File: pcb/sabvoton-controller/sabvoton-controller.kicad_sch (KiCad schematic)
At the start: 43 parts, among them J1 CONTROLLER_HALL, J2 CONN_MAIN, J3 ENGINE_HALL, J4 DISPLAY_CONNECTOR, Q1 BSS123, Q2 BSS123, Q3 BSS123, U1 ESP32-WROOM-32, U2 XL7015E1, U3 XL7015E1, U4 NCP1117-3.3_SOT223, U5 LM1117-1.8, U6 BTS4140N, U7 LM358

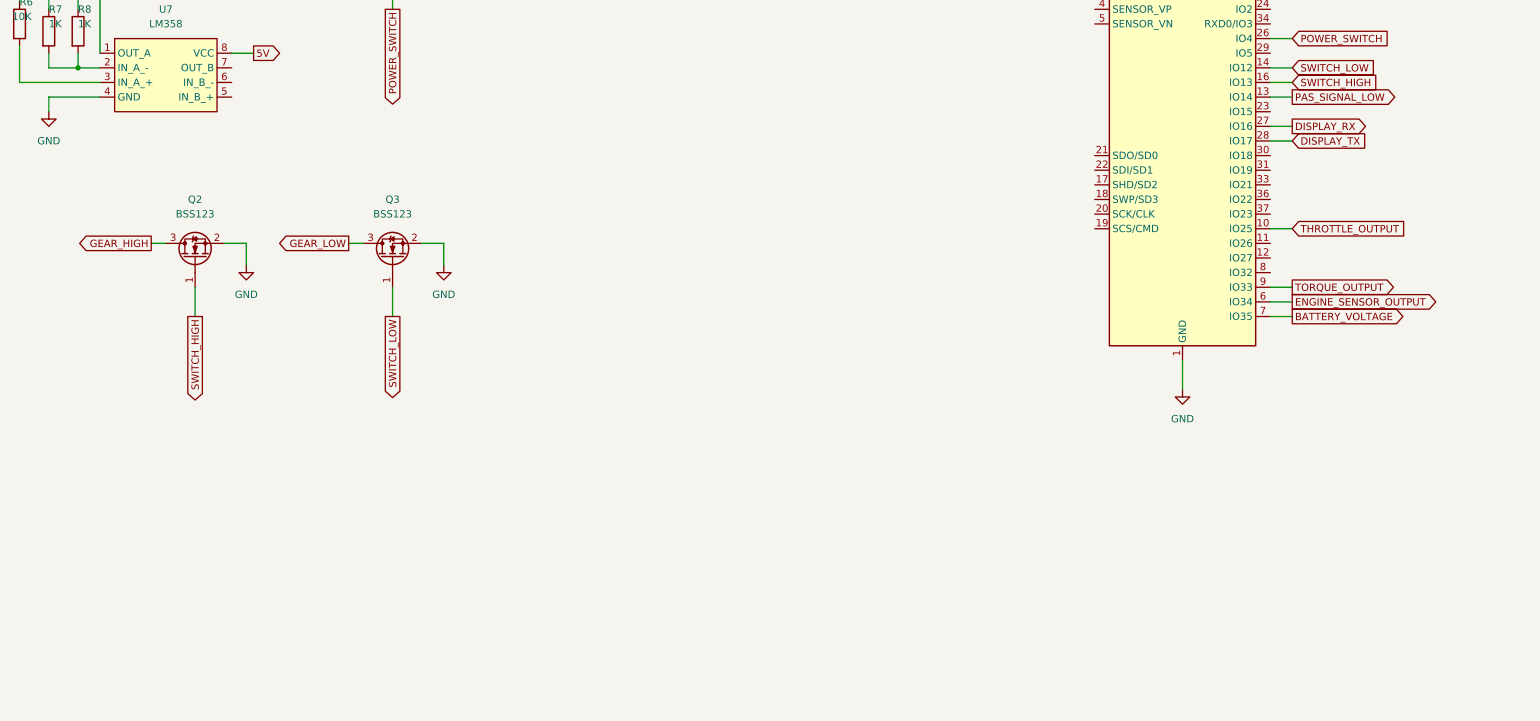
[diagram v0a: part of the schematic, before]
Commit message: Added soft start switch
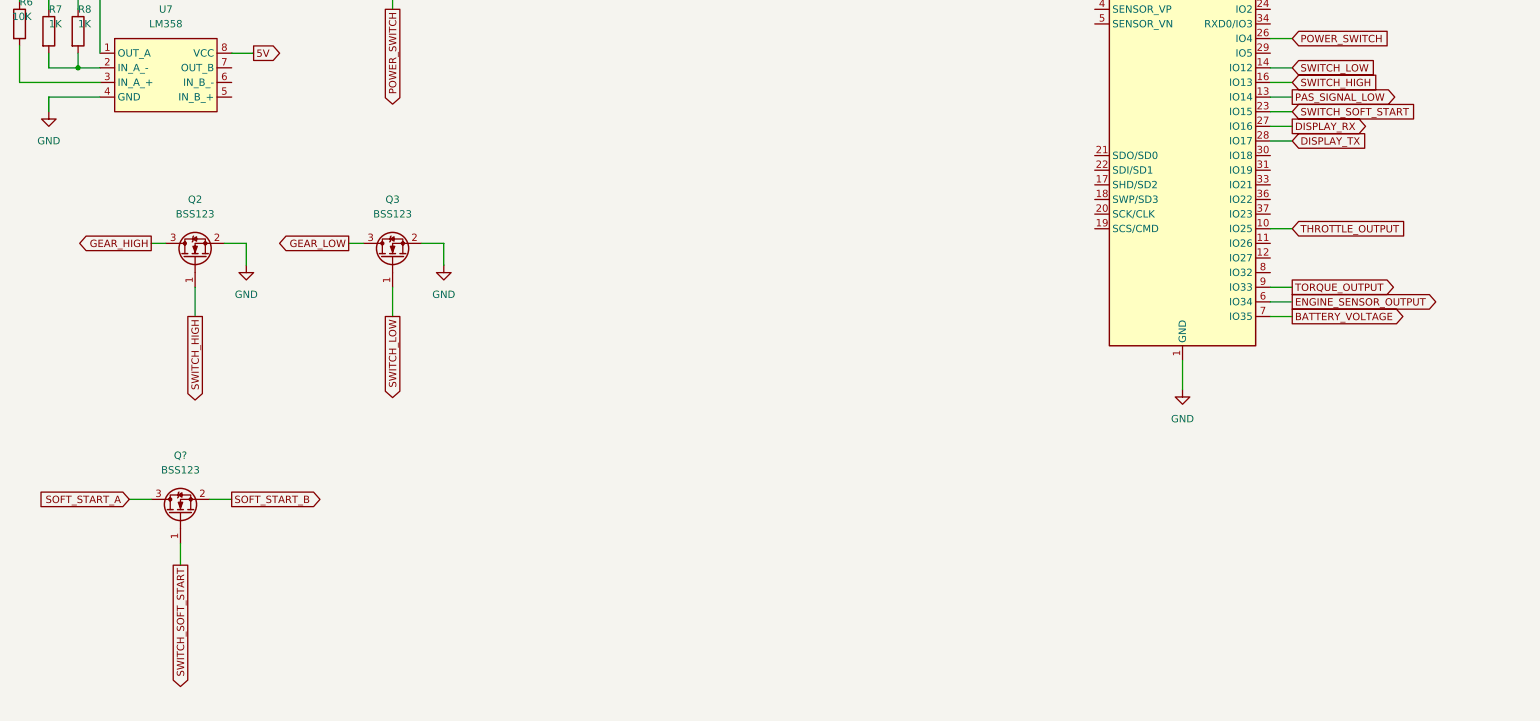
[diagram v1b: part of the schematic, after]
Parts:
- added Q?: BSS123, Package_TO_SOT_SMD:SOT-23, symbol Transistor_FET:BSS123
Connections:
- net SOFT_START_A: now also Q?.3 (D)
- net SOFT_START_B: now also Q?.2 (S)
- net SWITCH_SOFT_START: now reaches U1.23 (IO15)
- net SWITCH_SOFT_START: now also Q?.1 (G)
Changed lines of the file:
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@@
+    (stroke (width 0) (type default) (color 0 0 0 0))
+  )
+  (wire (pts (xy 209.55 219.71) (xy 213.36 219.71))
     (stroke (width 0) (type default) (color 0 0 0 0))
   )
@@
     (stroke (width 0) (type default) (color 0 0 0 0))
   )
+  (wire (pts (xy 204.47 227.33) (xy 204.47 231.14))
+    (stroke (width 0) (type default) (color 0 0 0 0))
+  )
   (wire (pts (xy 339.09 66.04) (xy 339.09 71.12))
     (stroke (width 0) (type default) (color 0 0 0 0))
@@
     (stroke (width 0) (type default) (color 0 0 0 0))
   )
+  (wire (pts (xy 393.7 152.4) (xy 397.51 152.4))
+    (stroke (width 0) (type default) (color 0 0 0 0))
+  )
   (wire (pts (xy 336.55 63.5) (xy 336.55 48.26))
     (stroke (width 0) (type default) (color 0 0 0 0))
@@
     (stroke (width 0) (type default) (color 0 0 0 0))
   )
+  (wire (pts (xy 195.58 219.71) (xy 199.39 219.71))
+    (stroke (width 0) (type default) (color 0 0 0 0))
+  )
   (wire (pts (xy 378.46 118.11) (xy 378.46 124.46))
     (stroke (width 0) (type default) (color 0 0 0 0))
@@
     )
   )
+  (global_label "SWITCH_SOFT_START" (shape input) (at 397.51 152.4 0) (fields_autoplaced)
+    (effects (font (size 1.27 1.27)) (justify left))
+    (property "Intersheet References" "${INTERSHEET_REFS}" (id 0) (at 418.7917 152.3206 0)
+      (effects (font (size 1.27 1.27)) (justify left) hide)
+    )
+  )
   (global_label "DISPLAY_TX" (shape output) (at 285.75 50.8 270) (fields_autoplaced)
     (effects (font (size 1.27 1.27)) (justify right))
@@
     )
   )
+  (global_label "SWITCH_SOFT_START" (shape output) (at 204.47 231.14 270) (fields_autoplaced)
+    (effects (font (size 1.27 1.27)) (justify right))
+    (property "Intersheet References" "${INTERSHEET_REFS}" (id 0) (at 204.3906 252.4217 90)
+      (effects (font (size 1.27 1.27)) (justify right) hide)
+    )
+  )
   (global_label "3.3V" (shape output) (at 378.46 118.11 90) (fields_autoplaced)
     (effects (font (size 1.27 1.27)) (justify left))
@@
     )
   )
+  (global_label "SOFT_START_A" (shape input) (at 195.58 219.71 180) (fields_autoplaced)
+    (effects (font (size 1.27 1.27)) (justify right))
+    (property "Intersheet References" "${INTERSHEET_REFS}" (id 0) (at 180.0436 219.6306 0)
+      (effects (font (size 1.27 1.27)) (justify right) hide)
+    )
+  )
   (global_label "PAS_SIGNAL" (shape output) (at 508 147.32 180) (fields_autoplaced)
     (effects (font (size 1.27 1.27)) (justify right))
@@
     (effects (font (size 1.27 1.27)) (justify left))
     (property "Intersheet References" "${INTERSHEET_REFS}" (id 0) (at 545.3079 147.2406 0)
+      (effects (font (size 1.27 1.27)) (justify left) hide)
+    )
+  )
+  (global_label "SOFT_START_B" (shape output) (at 213.36 219.71 0) (fields_autoplaced)
+    (effects (font (size 1.27 1.27)) (justify left))
+    (property "Intersheet References" "${INTERSHEET_REFS}" (id 0) (at 229.0779 219.6306 0)
       (effects (font (size 1.27 1.27)) (justify left) hide)
     )
@@
     (pin "3")
     (pin "4")
+  )
+  (symbol (lib_id "Transistor_FET:BSS123") (at 204.47 222.25 90) (unit 1)
+    (in_bom yes) (on_board yes) (fields_autoplaced)
+    (property "Reference" "Q?" (id 0) (at 204.47 212.09 90))
+    (property "Value" "BSS123" (id 1) (at 204.47 214.63 90))
+    (property "Footprint" "Package_TO_SOT_SMD:SOT-23" (id 2) (at 206.375 217.17 0)
+      (effects (font (size 1.27 1.27) italic) (justify left) hide)
+    )
+    (property "Datasheet" "http://www.diodes.com/assets/Datasheets/ds30366.pdf" (id 3) (at 204.47 222.25 0)
+      (effects (font (size 1.27 1.27)) (justify left) hide)
+    )
+    (pin "1")
+    (pin "2")
+    (pin "3")
   )
   (symbol (lib_id "Device:C") (at 544.83 104.14 0) (unit 1)
@@
       (reference "Q3") (unit 1) (value "BSS123") (footprint "Package_TO_SOT_SMD:SOT-23")
     )
+    (path "/733e1eb3-afcc-4a44-afac-d7ce4b6dac88"
+      (reference "Q?") (unit 1) (value "BSS123") (footprint "Package_TO_SOT_SMD:SOT-23")
+    )
     (path "/3c54a24c-10be-4236-a15f-1623c52b157c"

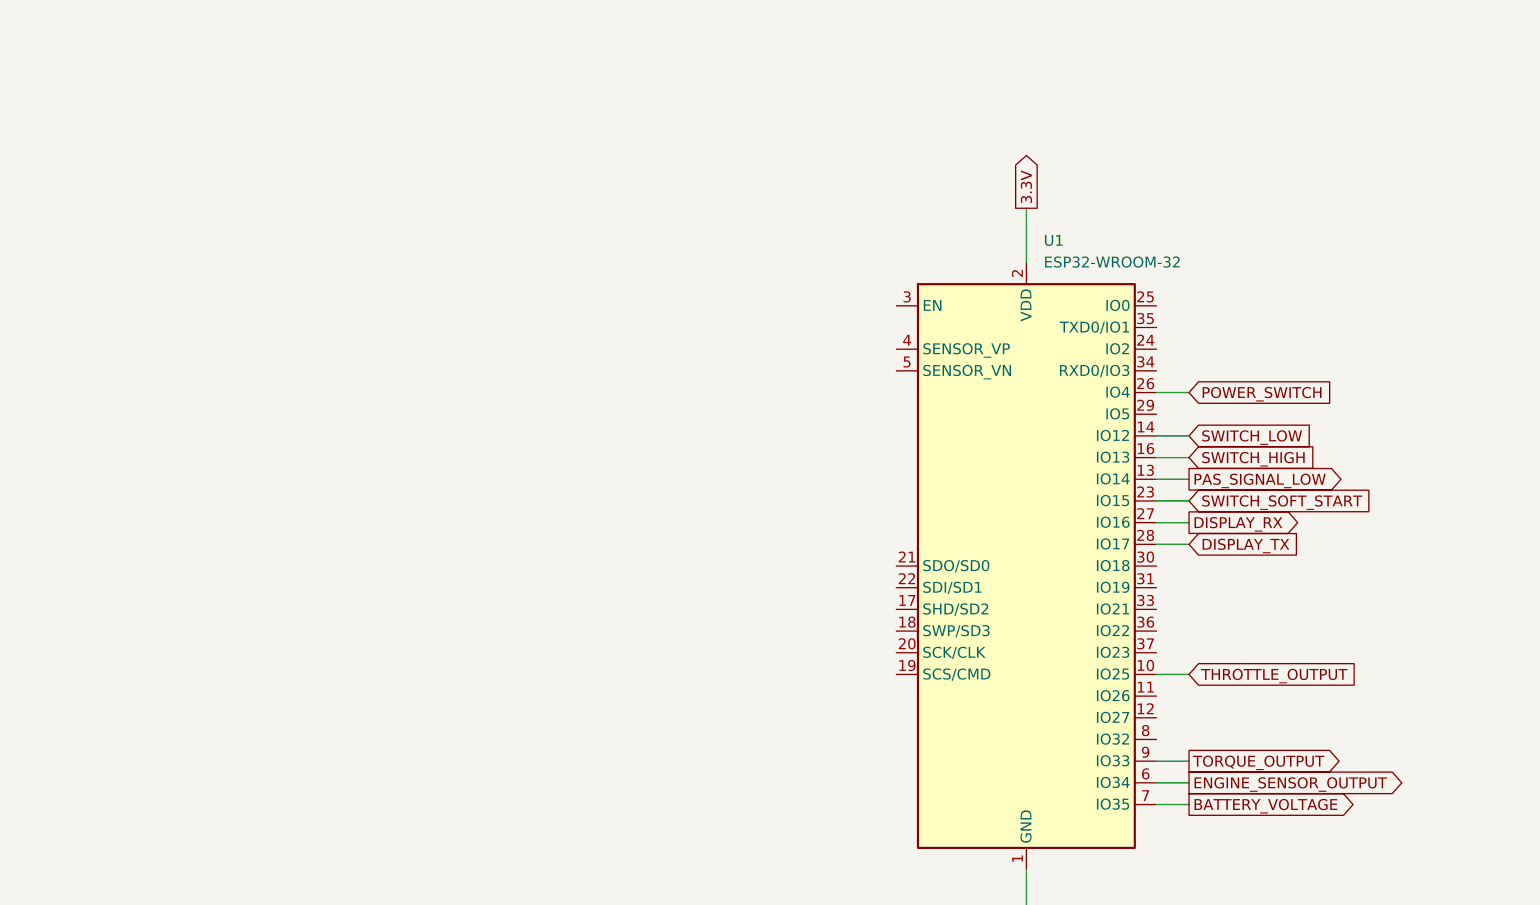
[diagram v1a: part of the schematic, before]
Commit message: Added battery & controller thermistor connections
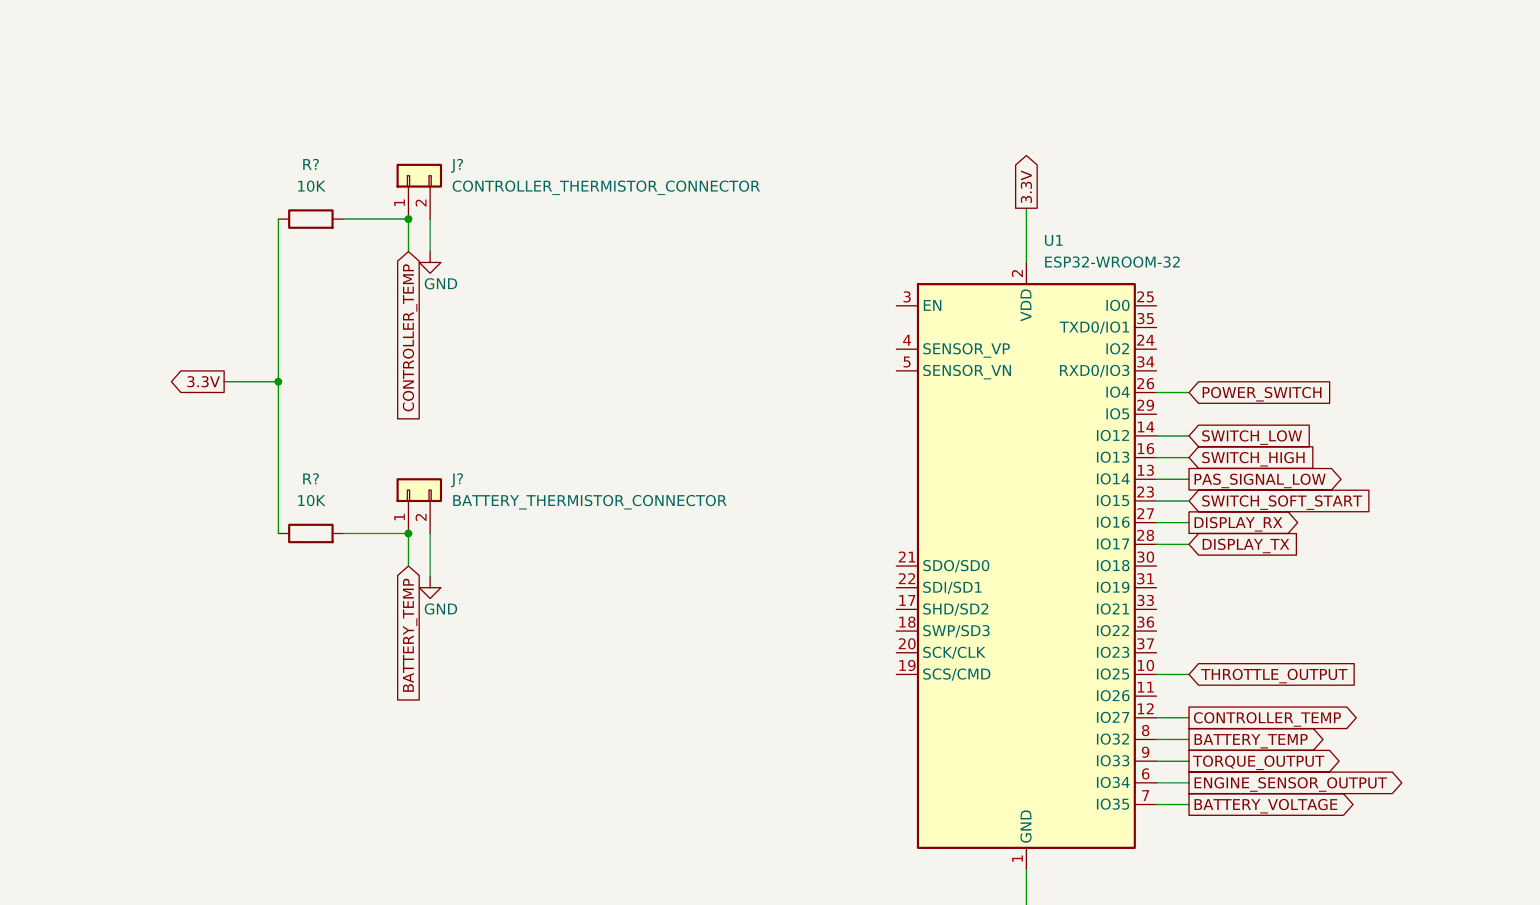
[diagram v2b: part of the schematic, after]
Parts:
- added J?: BATTERY_THERMISTOR_CONNECTOR, symbol Connector_Generic:Conn_01x02
- added J?: CONTROLLER_THERMISTOR_CONNECTOR, symbol Connector_Generic:Conn_01x02
- added R? (x2): 10K, symbol Device:R
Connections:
- net 3.3V: now also R?.1, R?.1
- net GND: now also J?.2 (Pin_2), J?.2 (Pin_2)
- net CONTROLLER_TEMP: now reaches U1.12 (IO27)
- net CONTROLLER_TEMP: now also J?.1 (Pin_1), R?.2
- net BATTERY_TEMP: now reaches U1.8 (IO32)
- net BATTERY_TEMP: now also J?.1 (Pin_1), R?.2
